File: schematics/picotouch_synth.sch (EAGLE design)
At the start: 100 parts, among them IC2 H11L1MS, J1 AUDIO-JACK-TRRS, J3 AUDIO-JACK-TRRS, J4 AUDIO-JACK-TRRS, U1 RASPBERRY_PICOSMD

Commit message: commit before fab
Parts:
- R10: value (none) -> 1M
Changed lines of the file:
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@@
 <part name="TP9" library="todstuff" library_urn="urn:adsk.eagle:library:1731349" deviceset="TOUCHPAD" device="A" package3d_urn="urn:adsk.eagle:package:27542649/4"/>
 <part name="GND10" library="supply1" library_urn="urn:adsk.eagle:library:371" deviceset="GND" device=""/>
-<part name="R10" library="rcl" library_urn="urn:adsk.eagle:library:334" deviceset="R-EU_" device="R0805" package3d_urn="urn:adsk.eagle:package:23553/2"/>
+<part name="R10" library="rcl" library_urn="urn:adsk.eagle:library:334" deviceset="R-EU_" device="R0805" package3d_urn="urn:adsk.eagle:package:23553/2" value="1M"/>
 <part name="TP10" library="todstuff" library_urn="urn:adsk.eagle:library:1731349" deviceset="TOUCHPAD" device="A" package3d_urn="urn:adsk.eagle:package:27542649/4"/>
 <part name="GND11" library="supply1" library_urn="urn:adsk.eagle:library:371" deviceset="GND" device=""/>

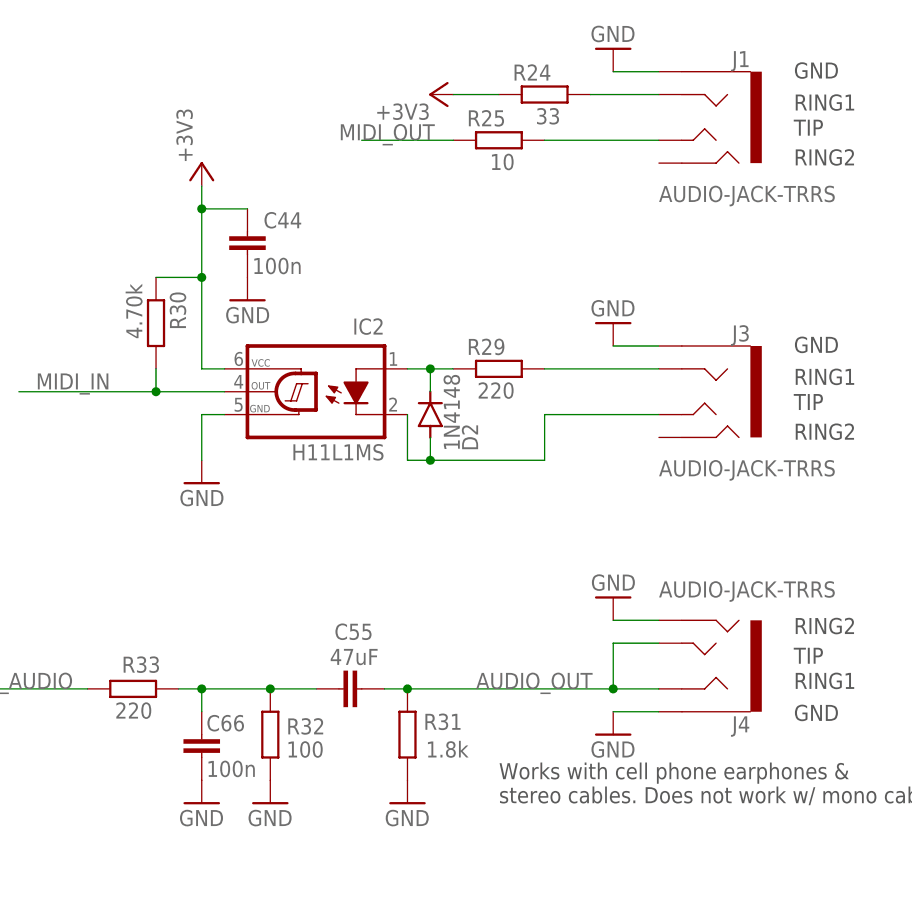
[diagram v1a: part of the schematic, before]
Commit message: moved topsilk to tNames so it renders
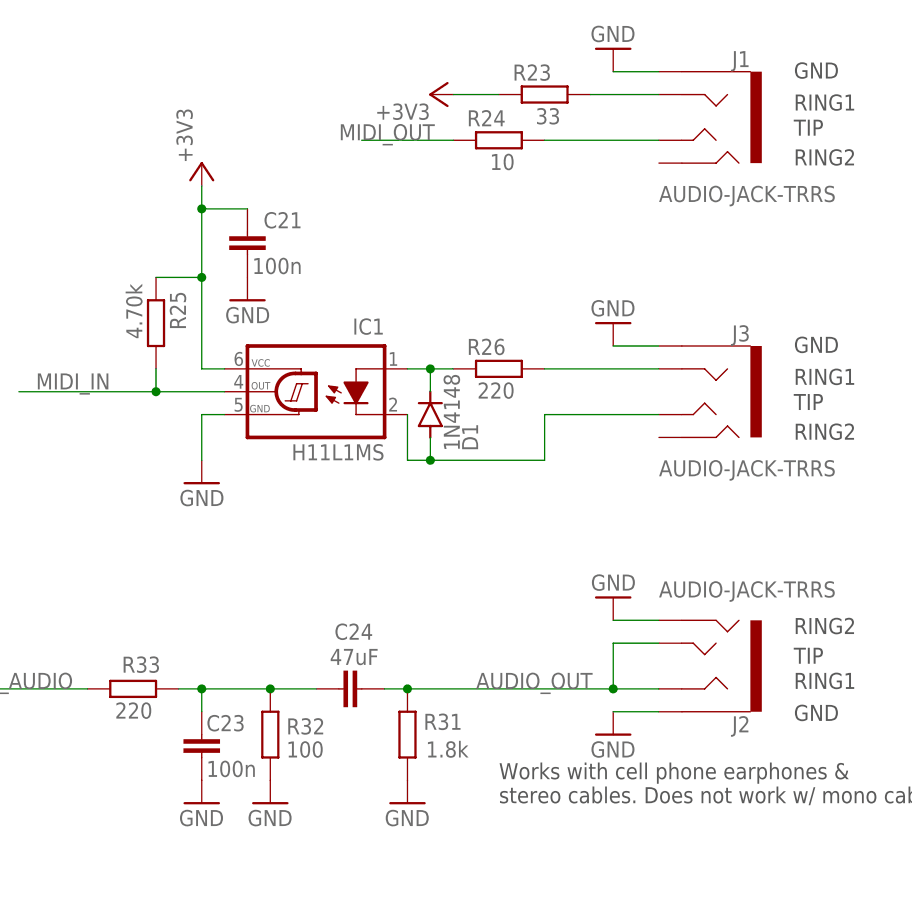
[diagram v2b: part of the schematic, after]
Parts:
- removed R30: 4.70k, rcl:R-EU_R0603
- added R23: 33, rcl:R-EU_R0603
- R24: value 33 -> 10
- R25: value 10 -> 4.70k
- renumbered C44 to C21, C55 to C24, C66 to C23, D2 to D1, IC2 to IC1, J4 to J2, R29 to R26
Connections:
- net +3V3: now also R23.1, R25.1; no longer R24.1, R30.1
- net MIDI_IN: now also R25.2; no longer R30.2
- net MIDI_OUT: now also R24.1; no longer R25.1
- net N$2: now also R24.2; no longer R25.2
- net N$6: now also R23.2; no longer R24.2
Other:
- moved on the sheet: R24, R25

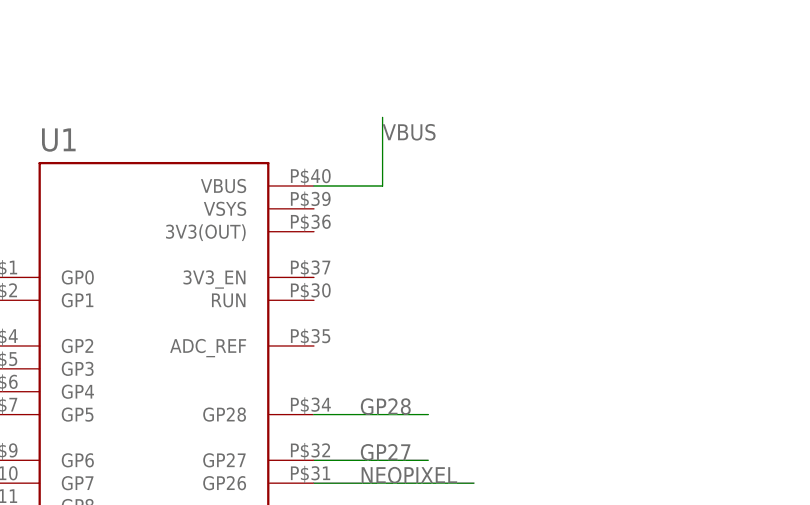
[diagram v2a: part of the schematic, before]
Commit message: forgot to wire 3v3. wow I am really dumb
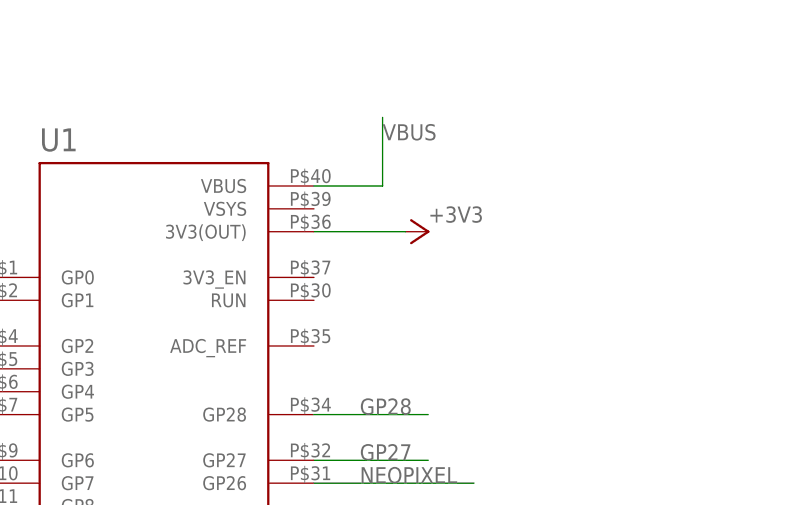
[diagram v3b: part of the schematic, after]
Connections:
- net +3V3: now also U1.3V3(OUT)
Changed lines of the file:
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@@
 <part name="R22" library="rcl" library_urn="urn:adsk.eagle:library:334" deviceset="R-EU_" device="R0603" package3d_urn="urn:adsk.eagle:package:23555/3" value="1M"/>
 <part name="GND25" library="supply1" library_urn="urn:adsk.eagle:library:371" deviceset="GND" device=""/>
+<part name="+3V42" library="supply1" library_urn="urn:adsk.eagle:library:371" deviceset="+3V3" device=""/>
 </parts>
 <sheets>
@@
 <attribute name="VALUE" x="2.54" y="-127" size="1.778" layer="96"/>
 </instance>
+<instance part="+3V42" gate="G$1" x="25.4" y="78.74" smashed="yes" rot="R270">
+<attribute name="VALUE" x="25.4" y="79.756" size="1.778" layer="96"/>
+</instance>
 </instances>
 <busses>
@@
 <pinref part="+3V44" gate="G$1" pin="+3V3"/>
 </segment>
-</net>
+<segment>
+<pinref part="U1" gate="U$1" pin="3V3(OUT)"/>
+<wire x1="12.7" y1="78.74" x2="22.86" y2="78.74" width="0.1524" layer="91"/>
+<pinref part="+3V42" gate="G$1" pin="+3V3"/>
+</segment>
+</net>
